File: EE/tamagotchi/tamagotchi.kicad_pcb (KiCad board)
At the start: 4 copper layers, 34.8 x 38.8 mm, 46 parts, among them J1 Conn_01x02_Male, J3 Conn_01x07, J7 TAG_CONNECT, J8 Conn_01x02_Male, P1 USB_C_Plug_USB2.0, Q1 Q_NMOS_GSD, Q2 Q_NMOS_GSD, Q4 Q_NMOS_GSD, Q5 Q_PMOS_GSD, SW2 TL1260BQRBLK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

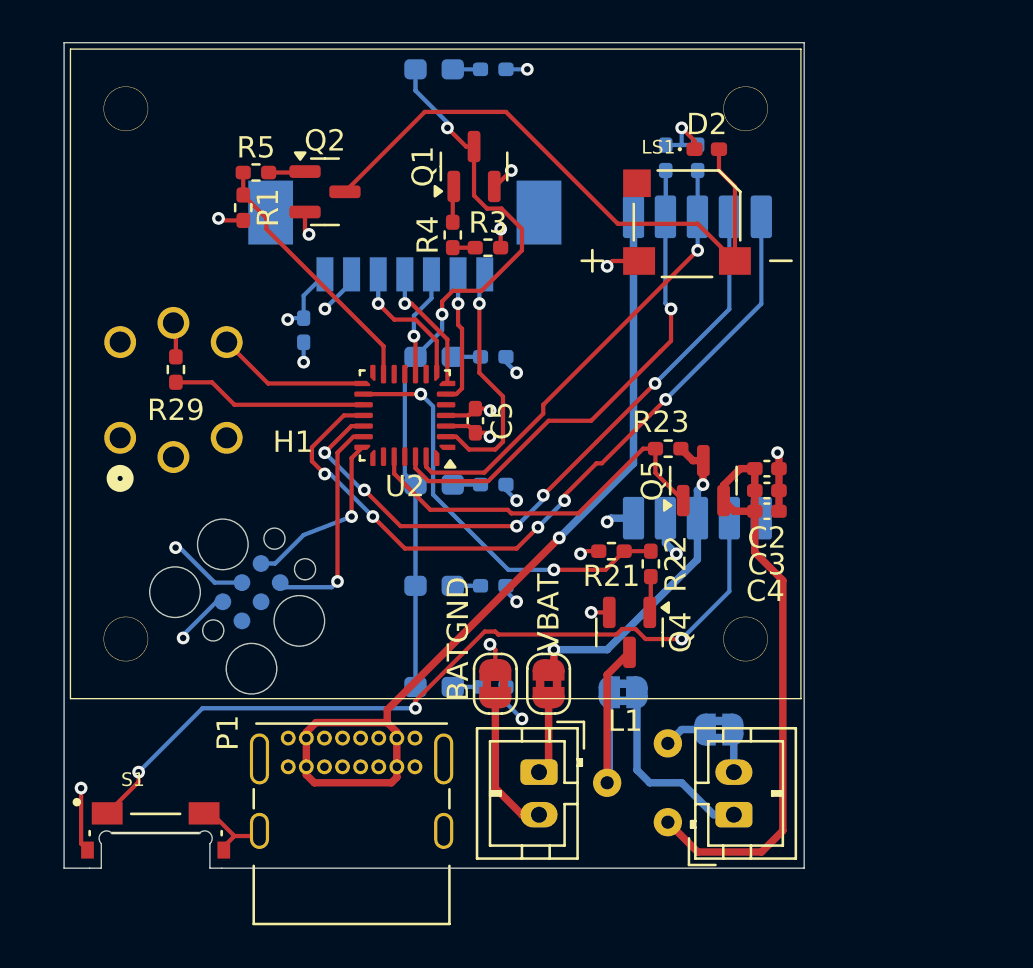
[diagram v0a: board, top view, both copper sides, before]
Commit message: Added pressure sensor. Re laid out board
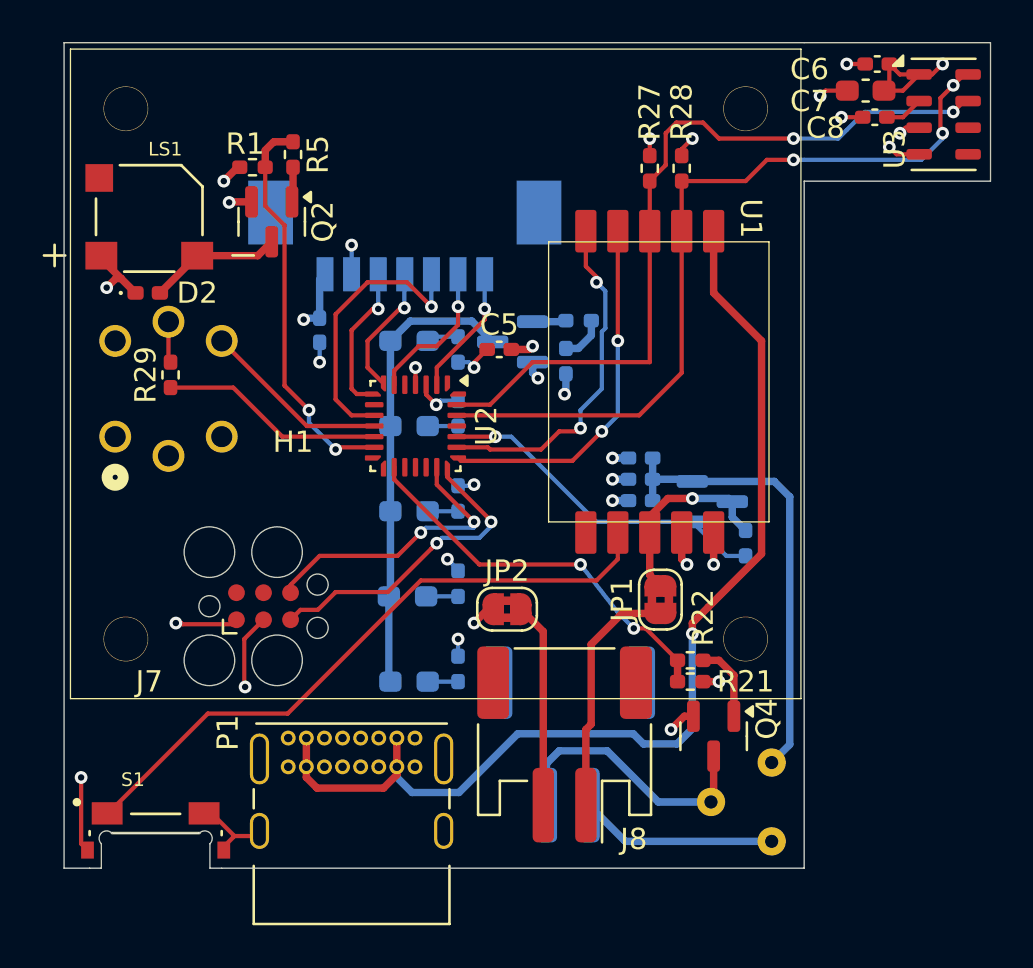
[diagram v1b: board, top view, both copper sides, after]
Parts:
- removed BATGND, UT+, UT-, VBAT: SolderJumper_2_Bridged, Jumper:SolderJumper-2_P1.3mm_Bridged2Bar_RoundedPad1.0x1.5mm
- added C6: 0.1u, Capacitor_SMD:C_0402_1005Metric_Pad0.74x0.62mm_HandSolder, F.Cu at (174.2, 72.0)
- added C7: 10u, Capacitor_SMD:C_0603_1608Metric_Pad1.08x0.95mm_HandSolder, F.Cu at (173.6, 73.2)
- added C8: 0.1u, Capacitor_SMD:C_0402_1005Metric_Pad0.74x0.62mm_HandSolder, F.Cu at (174.1, 74.5)
- added JP1: SolderJumper_2_Bridged, Jumper:SolderJumper-2_P1.3mm_Bridged2Bar_RoundedPad1.0x1.5mm, F.Cu at (164.0, 97.2)
- added JP2: SolderJumper_2_Bridged, Jumper:SolderJumper-2_P1.3mm_Bridged2Bar_RoundedPad1.0x1.5mm, F.Cu at (156.8, 97.6)
- added U3: MPL3115A2, Package_LGA:NXP_LGA-8_3x5mm_P1.25mm_H1.1mm, F.Cu at (177.3, 74.4)
- C2, C3, C4, L1, Q1, Q5, R23, R3, R4: moved to B.Cu
- J1: footprint Connector_JST:JST_PH_B2B-PH-K_1x02_P2.00mm_Vertical -> Connector_JST:JST_PH_S2B-PH-SM4-TB_1x02-1MP_P2.00mm_Horizontal; moved to B.Cu
- J7, R27, R28, U1: moved to F.Cu
- J8: footprint Connector_JST:JST_PH_B2B-PH-K_1x02_P2.00mm_Vertical -> Connector_JST:JST_PH_S2B-PH-SM4-TB_1x02-1MP_P2.00mm_Horizontal
- moved D2 27.1 mm to (139.9, 82.8)
- moved LS1 25.3 mm to (140.0, 79.2)
- moved D7 20.8 mm to (152.2, 93.0)
- moved R15 20.2 mm to (154.5, 92.4), turned to -90 degrees
- moved D9 16.3 mm to (152.2, 85.0)
- moved R17 15.9 mm to (154.5, 85.4), turned to 90 degrees
- moved D1 9.32 mm to (152.2, 101.0)
- moved R2 8.81 mm to (154.5, 100.4), turned to -90 degrees
- moved U1 8.79 mm to (169.0, 86.8)
- moved J1 8.47 mm to (159.7, 104.0), turned to 0 degrees
- moved Q1 8.43 mm to (157.1, 85.0), turned to 180 degrees
- moved R21 7.16 mm to (165.4, 101.0), turned to 0 degrees
- moved R4 7.15 mm to (160.2, 84.0), turned to 180 degrees
- moved R3 6.46 mm to (159.6, 86.0), turned to -90 degrees
- moved Q4 6.27 mm to (166.5, 103.6)
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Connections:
- net /MCU/SCL renamed /SCL
- net /MCU/SDA renamed /SDA
- J1 pad 1: Net-(J1-Pin_1) -> /Vape/UT_OUT-
- J1 pad 2: Net-(J1-Pin_2) -> /Vape/UT_OUT+
- U2 pad 11: unconnected-(U2-PA5-Pad11) -> /MCU/VAPE_SW
- U2 pad 12: unconnected-(U2-PA6-Pad12) -> /MCU/VAPE_LED
- U2 pad 15: /MCU/VAPE_SW -> unconnected-(U2-PB1-Pad15)
- U2 pad 17: /MCU/VAPE_LED -> unconnected-(U2-PC6-Pad17)
- U2 pad 18: /MCU/CE_N -> unconnected-(U2-PA9/PA11-Pad18)
- U2 pad 19: /MCU/INT_N -> unconnected-(U2-PA10/PA12-Pad19)
- U2 pad 22: unconnected-(U2-PA15-Pad22) -> /MCU/INT_N
- U2 pad 23: unconnected-(U2-PB3-Pad23) -> /MCU/CE_N
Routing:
- net Net-(D2-A): track 28.3 -> 6.25 mm
- net /MCU/CE_N: track 35.5 -> 16.4 mm, vias 5 -> 2
- net /SDA: track 21.7 -> 36.4 mm, vias 1 -> 2
- net /MCU/INT_N: track 31.4 -> 17.1 mm, vias 5 -> 2
- net /SCL: track 23.6 -> 37.2 mm, vias 1 -> 3
- net Net-(D1-K): track 35.0 -> 21.7 mm, vias 2 -> 0
- net Net-(J1-Pin_1): track 9.07 -> 0.00 mm
- net VBUS: track 41.8 -> 50.2 mm
- net /Display/CS: track 5.06 -> 13.2 mm
- net Net-(J8-Pin_1): track 3.69 -> 11.5 mm
- net /Power/SWITCH: track 37.9 -> 30.2 mm, vias 3 -> 0
- net /Vape/UT_OUT+: track 2.02 -> 9.28 mm
- net /Display/BUZZ_PWM: track 12.2 -> 18.7 mm, vias 0 -> 2
- net /Vape/VBAT_CONT: track 28.1 -> 21.6 mm
- net /MCU/SWCLK: track 8.42 -> 14.8 mm, vias 1 -> 2
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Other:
- board size 34.8 x 38.8 mm -> 43.5 x 38.8 mm
